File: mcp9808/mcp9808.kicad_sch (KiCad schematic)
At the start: 0 parts

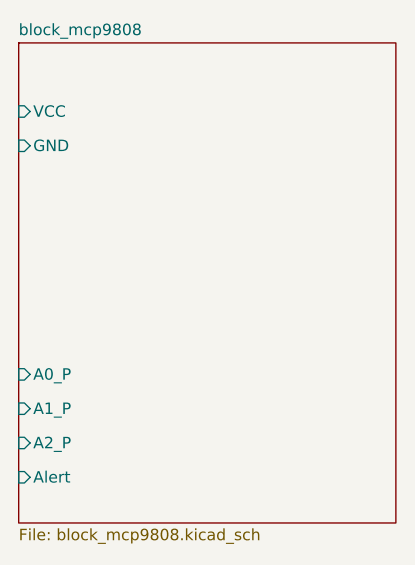
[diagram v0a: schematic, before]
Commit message: [Rushil] edited mcp9808 json with respect to the corrected ciruit
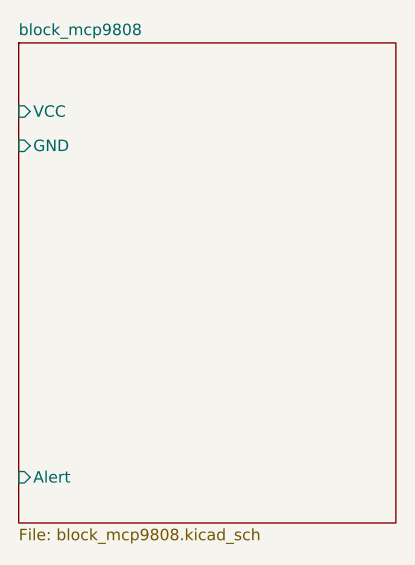
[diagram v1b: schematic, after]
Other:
- sheet block_mcp9808 ports: added none; removed A0_P, A1_P, A2_P
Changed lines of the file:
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@@
-			)
-		)
-		(pin "A0_P" input
-			(at 95.25 99.06 180)
-			(effects
-				(font
-					(size 1.27 1.27)
-				)
-				(justify left)
-			)
-		)
-		(pin "A1_P" input
-			(at 95.25 102.87 180)
-			(effects
-				(font
-					(size 1.27 1.27)
-				)
-				(justify left)
-			)
-		)
-		(pin "A2_P" input
-			(at 95.25 106.68 180)
-			(effects
-				(font
-					(size 1.27 1.27)
-				)
-				(justify left)
 			)
 		)

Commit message: [Rushil] corrected pcb added information on both schematic and pcb user drawing correct circuit of bno055
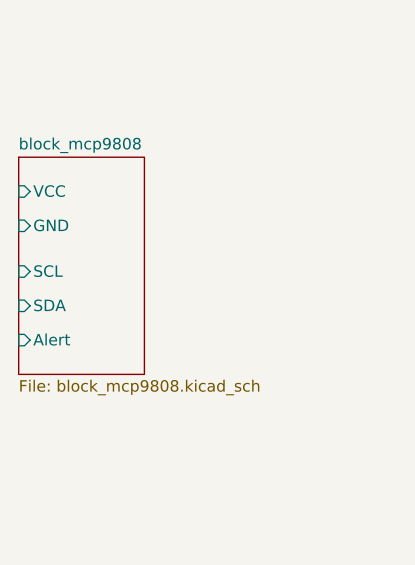
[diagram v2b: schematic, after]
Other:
- sheet block_mcp9808 ports: added SCL, SDA; removed none
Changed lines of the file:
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@@
 	(paper "A4")
 	(sheet
-		(at 95.25 62.23)
-		(size 41.91 53.34)
+		(at 95.25 74.93)
+		(size 13.97 24.13)
 		(exclude_from_sim no)
 		(in_bom yes)
@@
 		)
 		(property "Sheetname" "block_mcp9808"
-			(at 95.25 61.5184 0)
+			(at 95.25 74.2184 0)
 			(effects
 				(font
@@
 		)
 		(property "Sheetfile" "block_mcp9808.kicad_sch"
-			(at 95.25 116.1546 0)
+			(at 95.25 99.6446 0)
 			(effects
 				(font
@@
 		)
 		(pin "Alert" input
-			(at 95.25 110.49 180)
+			(at 95.25 95.25 180)
 			(effects
 				(font
@@
 		)
 		(pin "GND" input
-			(at 95.25 73.66 180)
+			(at 95.25 82.55 180)
 			(effects
 				(font
@@
 		)
 		(pin "VCC" input
-			(at 95.25 69.85 180)
+			(at 95.25 78.74 180)
 			(effects
 				(font
+					(size 1.27 1.27)
+				)
+				(justify left)
+			)
+		)
+		(pin "SCL" input
+			(at 95.25 87.63 180)
+			(effects
+				(font
+					(size 1.27 1.27)
+				)
+				(justify left)
+			)
+		)
+		(pin "SDA" input
+			(at 95.25 91.44 180)
+			(effects
+				(font

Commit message: Edited and finalized blocks MCP9809 and DS3231
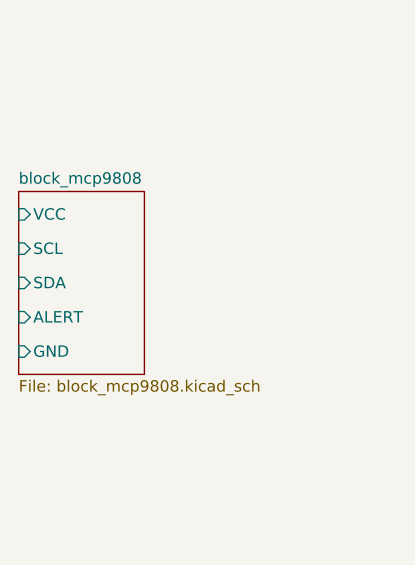
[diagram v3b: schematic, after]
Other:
- sheet block_mcp9808 ports: added ALERT; removed Alert
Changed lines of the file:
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@@
 	(paper "A4")
 	(sheet
-		(at 95.25 74.93)
-		(size 13.97 24.13)
+		(at 95.25 78.74)
+		(size 13.97 20.32)
 		(exclude_from_sim no)
 		(in_bom yes)
@@
 		)
 		(property "Sheetname" "block_mcp9808"
-			(at 95.25 74.2184 0)
+			(at 95.25 78.0284 0)
 			(effects
 				(font
@@
 			)
 		)
-		(pin "Alert" input
-			(at 95.25 95.25 180)
+		(pin "ALERT" input
+			(at 95.25 92.71 180)
 			(effects
 				(font
@@
 		)
 		(pin "GND" input
-			(at 95.25 82.55 180)
+			(at 95.25 96.52 180)
 			(effects
 				(font
@@
 		)
 		(pin "VCC" input
-			(at 95.25 78.74 180)
+			(at 95.25 81.28 180)
 			(effects
 				(font
@@
 		)
 		(pin "SCL" input
-			(at 95.25 87.63 180)
+			(at 95.25 85.09 180)
 			(effects
 				(font
@@
 		)
 		(pin "SDA" input
-			(at 95.25 91.44 180)
+			(at 95.25 88.9 180)
 			(effects
 				(font
